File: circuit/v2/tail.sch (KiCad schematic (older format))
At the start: 44 parts, among them J11 UART, J19 LiPo, J25 USB_OTG, J9 DEBUG, Q1 Q_NMOS_GSD, SW1 SW_SPDT, U1 DWM1000, U2 EFM32HG222F64, U3 MC3630, U4 XC6215B332NR, U5 MCP73831-2-OT, Y1 32.768kHz CFPX-217 20ppm 7pF

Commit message: tail: minor tweaks
Signed-off-by: Gavan Fantom <gavan.fantom@unipart.io>
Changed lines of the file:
@@
 $EndComp
 $Comp
-L GND #PWR16
+L GND #PWR01
 U 1 1 58D90344
 P 8650 2850
-F 0 "#PWR16" H 8650 2600 50  0001 C CNN
+F 0 "#PWR01" H 8650 2600 50  0001 C CNN
 F 1 "GND" H 8650 2700 50  0000 C CNN
 F 2 "" H 8650 2850 50  0001 C CNN
@@
 $EndComp
 $Comp
-L +BATT #PWR12
+L +BATT #PWR02
 U 1 1 58D90443
 P 6950 2400
-F 0 "#PWR12" H 6950 2250 50  0001 C CNN
+F 0 "#PWR02" H 6950 2250 50  0001 C CNN
 F 1 "+BATT" H 6950 2540 50  0000 C CNN
 F 2 "" H 6950 2400 50  0001 C CNN
@@
 $EndComp
 $Comp
-L +BATT #PWR15
+L +BATT #PWR03
 U 1 1 58D91168
-P 8150 5100
-F 0 "#PWR15" H 8150 4950 50  0001 C CNN
-F 1 "+BATT" H 8150 5240 50  0000 C CNN
-F 2 "" H 8150 5100 50  0001 C CNN
-F 3 "" H 8150 5100 50  0001 C CNN
-	1    8150 5100
+P 7900 5100
+F 0 "#PWR03" H 7900 4950 50  0001 C CNN
+F 1 "+BATT" H 7900 5240 50  0000 C CNN
+F 2 "" H 7900 5100 50  0001 C CNN
+F 3 "" H 7900 5100 50  0001 C CNN
+	1    7900 5100
 	1    0    0    -1
 $EndComp
@@
 $EndComp
 $Comp
-L GND #PWR11
+L GND #PWR04
 U 1 1 58E2BE94
 P 6750 6700
-F 0 "#PWR11" H 6750 6450 50  0001 C CNN
+F 0 "#PWR04" H 6750 6450 50  0001 C CNN
 F 1 "GND" H 6750 6550 50  0000 C CNN
 F 2 "" H 6750 6700 50  0001 C CNN
@@
 $EndComp
 $Comp
-L GND #PWR7
+L GND #PWR05
 U 1 1 58E32705
 P 3750 2550
-F 0 "#PWR7" H 3750 2300 50  0001 C CNN
+F 0 "#PWR05" H 3750 2300 50  0001 C CNN
 F 1 "GND" H 3750 2400 50  0000 C CNN
 F 2 "" H 3750 2550 50  0001 C CNN
@@
 $EndComp
 $Comp
-L GND #PWR13
+L GND #PWR06
 U 1 1 58E5097D
 P 6950 3600
-F 0 "#PWR13" H 6950 3350 50  0001 C CNN
+F 0 "#PWR06" H 6950 3350 50  0001 C CNN
 F 1 "GND" H 6950 3450 50  0000 C CNN
 F 2 "" H 6950 3600 50  0001 C CNN
@@
 $EndComp
 $Comp
-L GND #PWR17
+L GND #PWR07
 U 1 1 58E581CA
 P 8750 4650
-F 0 "#PWR17" H 8750 4400 50  0001 C CNN
+F 0 "#PWR07" H 8750 4400 50  0001 C CNN
 F 1 "GND" H 8750 4500 50  0000 C CNN
 F 2 "" H 8750 4650 50  0001 C CNN
@@
 $EndComp
 $Comp
-L GND #PWR18
+L GND #PWR08
 U 1 1 58E5823C
 P 10300 5400
-F 0 "#PWR18" H 10300 5150 50  0001 C CNN
+F 0 "#PWR08" H 10300 5150 50  0001 C CNN
 F 1 "GND" H 10300 5250 50  0000 C CNN
 F 2 "" H 10300 5400 50  0001 C CNN
@@
 $EndComp
 $Comp
-L GND #PWR14
+L GND #PWR09
 U 1 1 58E62DAE
 P 7200 4150
-F 0 "#PWR14" H 7200 3900 50  0001 C CNN
+F 0 "#PWR09" H 7200 3900 50  0001 C CNN
 F 1 "GND" H 7200 4000 50  0000 C CNN
 F 2 "" H 7200 4150 50  0001 C CNN
@@
 $EndComp
 $Comp
-L GND #PWR10
+L GND #PWR010
 U 1 1 58ECBC0F
 P 5250 5000
-F 0 "#PWR10" H 5250 4750 50  0001 C CNN
+F 0 "#PWR010" H 5250 4750 50  0001 C CNN
 F 1 "GND" H 5250 4850 50  0000 C CNN
 F 2 "" H 5250 5000 50  0001 C CNN
@@
 $EndComp
 $Comp
-L GND #PWR6
+L GND #PWR011
 U 1 1 58ECC8B8
 P 2450 6250
-F 0 "#PWR6" H 2450 6000 50  0001 C CNN
+F 0 "#PWR011" H 2450 6000 50  0001 C CNN
 F 1 "GND" H 2450 6100 50  0000 C CNN
 F 2 "" H 2450 6250 50  0001 C CNN
@@
 $EndComp
 $Comp
-L GND #PWR2
+L GND #PWR012
 U 1 1 58ECC92E
 P 950 5150
-F 0 "#PWR2" H 950 4900 50  0001 C CNN
+F 0 "#PWR012" H 950 4900 50  0001 C CNN
 F 1 "GND" H 950 5000 50  0000 C CNN
 F 2 "" H 950 5150 50  0001 C CNN
@@
 $EndComp
 $Comp
-L GND #PWR5
+L GND #PWR013
 U 1 1 58ECCA91
 P 1700 3950
-F 0 "#PWR5" H 1700 3700 50  0001 C CNN
+F 0 "#PWR013" H 1700 3700 50  0001 C CNN
 F 1 "GND" H 1700 3800 50  0000 C CNN
 F 2 "" H 1700 3950 50  0001 C CNN
@@
 $EndComp
 $Comp
-L GND #PWR3
+L GND #PWR014
 U 1 1 58ECF8A7
 P 1050 7550
-F 0 "#PWR3" H 1050 7300 50  0001 C CNN
+F 0 "#PWR014" H 1050 7300 50  0001 C CNN
 F 1 "GND" H 1050 7400 50  0000 C CNN
 F 2 "" H 1050 7550 50  0001 C CNN
@@
 $EndComp
 $Comp
-L GND #PWR8
+L GND #PWR015
 U 1 1 58ED2393
 P 4250 5600
-F 0 "#PWR8" H 4250 5350 50  0001 C CNN
+F 0 "#PWR015" H 4250 5350 50  0001 C CNN
 F 1 "GND" H 4250 5450 50  0000 C CNN
 F 2 "" H 4250 5600 50  0001 C CNN
@@
 $EndComp
 $Comp
-L GND #PWR1
+L GND #PWR016
 U 1 1 58ED2E64
 P 900 6150
-F 0 "#PWR1" H 900 5900 50  0001 C CNN
+F 0 "#PWR016" H 900 5900 50  0001 C CNN
 F 1 "GND" H 900 6000 50  0000 C CNN
 F 2 "" H 900 6150 50  0001 C CNN
@@
 $EndComp
 $Comp
-L GND #PWR4
+L GND #PWR017
 U 1 1 58ED2EF0
 P 1400 6150
-F 0 "#PWR4" H 1400 5900 50  0001 C CNN
+F 0 "#PWR017" H 1400 5900 50  0001 C CNN
 F 1 "GND" H 1400 6000 50  0000 C CNN
 F 2 "" H 1400 6150 50  0001 C CNN
@@
 $EndComp
 $Comp
-L PWR_FLAG #FLG2
+L PWR_FLAG #FLG018
 U 1 1 58EFDE28
 P 10700 3950
-F 0 "#FLG2" H 10700 4025 50  0001 C CNN
+F 0 "#FLG018" H 10700 4025 50  0001 C CNN
 F 1 "PWR_FLAG" H 10700 4100 50  0000 C CNN
 F 2 "" H 10700 3950 50  0001 C CNN
@@
 $EndComp
 $Comp
-L PWR_FLAG #FLG1
+L PWR_FLAG #FLG019
 U 1 1 58F0C76B
 P 9950 5400
-F 0 "#FLG1" H 9950 5475 50  0001 C CNN
+F 0 "#FLG019" H 9950 5475 50  0001 C CNN
 F 1 "PWR_FLAG" H 9950 5550 50  0000 C CNN
 F 2 "" H 9950 5400 50  0001 C CNN
@@
 $EndComp
 $Comp
-L GND #PWR9
+L GND #PWR020
 U 1 1 590A2FEB
 P 4850 6800
-F 0 "#PWR9" H 4850 6550 50  0001 C CNN
+F 0 "#PWR020" H 4850 6550 50  0001 C CNN
 F 1 "GND" H 4850 6650 50  0000 C CNN
 F 2 "" H 4850 6800 50  0001 C CNN
@@
 	1500 5100 950  5100
 Wire Wire Line
-	5250 4600 5250 4700
-Wire Wire Line
-	5250 4700 5250 4800
-Wire Wire Line
-	5250 4800 5250 4900
-Wire Wire Line
-	5250 4900 5250 5000
+	5250 4600 5250 5000
 Wire Wire Line
 	9850 4250 9850 5050
@@
 	8750 3950 8750 4050
 Wire Wire Line
-	9150 4250 9300 4250
-Wire Wire Line
-	9300 4250 9850 4250
+	9150 4250 9850 4250
 Wire Wire Line
 	8250 4450 8250 4650
@@
 	8250 3950 8250 4250
 Wire Wire Line
-	8250 3950 8750 3950
-Wire Wire Line
-	8750 3950 9550 3950
-Wire Wire Line
-	9550 3950 10700 3950
+	8250 3950 10700 3950
 Wire Wire Line
 	9150 4450 9550 4450
@@
 	9300 4250 9300 4400
 Wire Wire Line
-	8250 4650 8350 4650
-Wire Wire Line
-	8350 4650 8750 4650
-Wire Wire Line
-	8750 4650 9300 4650
+	8250 4650 9300 4650
 Wire Wire Line
 	6950 3250 6650 3250
 Wire Wire Line
-	6950 3200 6950 3250
-Wire Wire Line
-	6950 3250 6950 3300
-Wire Wire Line
-	1000 1550 1150 1550
-Wire Wire Line
-	1150 1550 1500 1550
+	6950 3200 6950 3300
+Wire Wire Line
+	1000 1550 1500 1550
 Wire Wire Line
 	1500 1550 1500 1450
@@
 	3750 1250 3300 1250
 Wire Wire Line
-	3750 2550 3750 1250
-Wire Wire Line
-	3750 1250 3750 1050
-Wire Wire Line
-	3750 1050 3750 950
+	3750 2550 3750 950
 Wire Wire Line
 	3750 950  3300 950
@@
 	1300 1650 1500 1650
 Wire Wire Line
-	1300 1650 1300 1750
-Wire Wire Line
-	1300 1750 1300 2550
-Wire Wire Line
-	1300 2550 1800 2550
-Wire Wire Line
-	1800 2550 2800 2550
-Wire Wire Line
-	2800 2550 3550 2550
-Wire Wire Line
-	3550 2550 3750 2550
+	1300 1650 1300 2550
+Wire Wire Line
+	1300 2550 3750 2550
 Wire Wire Line
 	2800 2350 2800 2550
@@
 	6150 6800 6300 6800
 Wire Wire Line
-	6150 6600 6300 6600
-Wire Wire Line
-	6300 6600 6750 6600
+	6150 6600 6750 6600
 Wire Wire Line
 	4750 6700 4850 6700
@@
 	6150 7400 4750 7400
 Wire Wire Line
-	6150 6800 6150 7250
-Wire Wire Line
-	6150 7250 6150 7400
+	6150 6800 6150 7400
 Wire Wire Line
 	8150 2400 8150 2550
@@
 	8150 2550 8200 2550
 Wire Wire Line
-	6950 2400 7750 2400
-Wire Wire Line
-	7750 2400 8150 2400
-Wire Wire Line
-	8150 2400 8200 2400
+	6950 2400 8200 2400
 Wire Wire Line
 	10700 3950 10700 4800
@@
 	8800 5400 8800 5300
 Wire Wire Line
-	8800 5400 9950 5400
-Wire Wire Line
-	9950 5400 10300 5400
-Wire Wire Line
-	10300 5400 10400 5400
+	8800 5400 10400 5400
 Wire Wire Line
 	7750 2850 7750 2700
@@
 	9100 2850 9100 2700
 Wire Wire Line
-	7750 2850 8650 2850
-Wire Wire Line
-	8650 2850 9100 2850
-Wire Wire Line
-	9100 1550 9100 1700
-Wire Wire Line
-	9100 1700 9100 1850
-Wire Wire Line
-	9100 1850 9100 2000
-Wire Wire Line
-	9100 2000 9100 2400
-Wire Wire Line
-	9100 2400 9100 2500
+	7750 2850 9100 2850
+Wire Wire Line
+	9100 1550 9100 2500
 Wire Wire Line
 	7750 2500 7750 2400
 Wire Wire Line
-	1050 7550 1450 7550
-Wire Wire Line
-	1450 7550 1700 7550
-Wire Wire Line
-	1700 7550 1950 7550
-Wire Wire Line
-	1950 7550 2200 7550
-Wire Wire Line
-	2200 7550 2450 7550
-Wire Wire Line
-	2450 7550 2700 7550
-Wire Wire Line
-	2700 7550 2950 7550
-Wire Wire Line
-	1200 7250 1450 7250
-Wire Wire Line
-	1450 7250 1700 7250
-Wire Wire Line
-	1700 7250 1950 7250
-Wire Wire Line
-	1950 7250 2200 7250
-Wire Wire Line
-	2200 7250 2450 7250
-Wire Wire Line
-	2450 7250 2700 7250
-Wire Wire Line
-	2700 7250 2950 7250
+	1050 7550 2950 7550
+Wire Wire Line
+	1200 7250 2950 7250
 Wire Wire Line
 	1450 7250 1450 7300
@@
 	2950 6350 2950 6250
 Wire Wire Line
-	2850 6350 2900 6350
-Wire Wire Line
-	2900 6350 2950 6350
+	2850 6350 2950 6350
 Wire Wire Line
 	2850 6350 2850 6250
@@
 	2900 6350 2900 6450
 Wire Wire Line
-	1250 5800 1400 5800
-Wire Wire Line
-	1400 5800 1500 5800
+	1250 5800 1500 5800
 Wire Wire Line
 	1400 5800 1400 5950
@@
 	1050 5800 900  5800
 Wire Wire Line
-	900  5700 900  5800
-Wire Wire Line
-	900  5800 900  5950
+	900  5700 900  5950
 Wire Wire Line
 	1500 5700 900  5700
 Wire Wire Line
-	1800 2550 1800 3050
-Wire Wire Line
-	1800 3050 1800 3400
+	1800 2550 1800 3400
 Wire Wire Line
 	2700 3050 3050 3050
@@
 	2400 3050 2300 3050
 Wire Wire Line
-	3550 2550 3550 3050
-Wire Wire Line
-	3550 3050 3550 3400
+	3550 2550 3550 3400
 Wire Wire Line
 	1150 1750 1300 1750
@@
 	8800 5200 8700 5200
 Wire Wire Line
-	8150 5100 8300 5100
+	7900 5100 8300 5100
 NoConn ~ 8300 5300
+$Comp
+L PWR_FLAG #FLG021
+U 1 1 5BB39745
+P 8250 5100
+F 0 "#FLG021" H 8250 5175 50  0001 C CNN
+F 1 "PWR_FLAG" H 8250 5250 50  0000 C CNN
+F 2 "" H 8250 5100 50  0001 C CNN
+F 3 "" H 8250 5100 50  0001 C CNN
+	1    8250 5100
+	1    0    0    -1
+$EndComp
+Connection ~ 8250 5100
 $EndSCHEMATC

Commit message: tail: More detail for SSSS811101 slide switch
This involves correcting the schematic and the symbol to match up the
pin numbering with the datasheet, and to add a case/body connection.

Signed-off-by: Gavan Fantom <gavan.fantom@unipart.io>
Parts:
- SW1: footprint (none) -> tail:SWITCH_SSSS811101; symbol SW_SPDT -> SW_SPDT_SSSS8
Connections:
- net +BATT: now also SW1.1 (B); no longer SW1.3 (C)
- net GND: now also SW1.4 (Body)
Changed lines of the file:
@@
 L +BATT #PWR03
 U 1 1 58D91168
-P 7900 5100
-F 0 "#PWR03" H 7900 4950 50  0001 C CNN
-F 1 "+BATT" H 7900 5240 50  0000 C CNN
-F 2 "" H 7900 5100 50  0001 C CNN
-F 3 "" H 7900 5100 50  0001 C CNN
-	1    7900 5100
+P 8100 5300
+F 0 "#PWR03" H 8100 5150 50  0001 C CNN
+F 1 "+BATT" H 8100 5440 50  0000 C CNN
+F 2 "" H 8100 5300 50  0001 C CNN
+F 3 "" H 8100 5300 50  0001 C CNN
+	1    8100 5300
 	1    0    0    -1
 $EndComp
@@
 NoConn ~ 2350 6250
 $Comp
-L SW_SPDT SW1
+L SW_SPDT_SSSS8 SW1
 U 1 1 5BB37913
 P 8500 5200
-F 0 "SW1" H 8450 5050 50  0000 C CNN
-F 1 "SW_SPDT" H 8450 5400 50  0000 C CNN
-F 2 "" H 8500 5200 50  0001 C CNN
+F 0 "SW1" H 8450 5400 50  0000 C CNN
+F 1 "SW_SPDT" H 8500 5000 50  0000 C CNN
+F 2 "tail:SWITCH_SSSS811101" H 8500 5200 50  0001 C CNN
 F 3 "" H 8500 5200 50  0001 C CNN
 F 4 "ALPS" H 8500 5200 60  0001 C CNN "MFR"
@@
 F 7 "688-SSSS811101" H 8500 5200 60  0001 C CNN "SPN"
 	1    8500 5200
-	-1   0    0    1
+	-1   0    0    -1
 $EndComp
 Wire Wire Line
 	8800 5200 8700 5200
 Wire Wire Line
-	7900 5100 8300 5100
-NoConn ~ 8300 5300
+	8100 5300 8300 5300
+NoConn ~ 8300 5100
 $Comp
 L PWR_FLAG #FLG021
 U 1 1 5BB39745
-P 8250 5100
-F 0 "#FLG021" H 8250 5175 50  0001 C CNN
-F 1 "PWR_FLAG" H 8250 5250 50  0000 C CNN
-F 2 "" H 8250 5100 50  0001 C CNN
-F 3 "" H 8250 5100 50  0001 C CNN
-	1    8250 5100
-	1    0    0    -1
-$EndComp
-Connection ~ 8250 5100
+P 8100 5300
+F 0 "#FLG021" H 8100 5375 50  0001 C CNN
+F 1 "PWR_FLAG" H 8100 5450 50  0000 C CNN
+F 2 "" H 8100 5300 50  0001 C CNN
+F 3 "" H 8100 5300 50  0001 C CNN
+	1    8100 5300
+	-1   0    0    1
+$EndComp
+Connection ~ 8100 5300
+$Comp
+L GND #PWR022
+U 1 1 5BB3B459
+P 8750 5450
+F 0 "#PWR022" H 8750 5200 50  0001 C CNN
+F 1 "GND" H 8750 5300 50  0000 C CNN
+F 2 "" H 8750 5450 50  0001 C CNN
+F 3 "" H 8750 5450 50  0001 C CNN
+	1    8750 5450
+	1    0    0    -1
+$EndComp
+Wire Wire Line
+	8700 5300 8750 5300
+Wire Wire Line
+	8750 5300 8750 5450
 $EndSCHEMATC

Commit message: tail: Route PCB
Signed-off-by: Gavan Fantom <gavan.fantom@unipart.io>
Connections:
- net +BATT: now also SW1.2 (C); no longer SW1.1 (B)
- net at C18.1, J19.1 (P1), U5.3 (Vbat): now also SW1.1 (B); no longer SW1.2 (C)
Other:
- moved on the sheet: SW1
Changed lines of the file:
@@
 L +BATT #PWR03
 U 1 1 58D91168
-P 8100 5300
-F 0 "#PWR03" H 8100 5150 50  0001 C CNN
-F 1 "+BATT" H 8100 5440 50  0000 C CNN
-F 2 "" H 8100 5300 50  0001 C CNN
-F 3 "" H 8100 5300 50  0001 C CNN
-	1    8100 5300
+P 8000 5100
+F 0 "#PWR03" H 8000 4950 50  0001 C CNN
+F 1 "+BATT" H 8000 5240 50  0000 C CNN
+F 2 "" H 8000 5100 50  0001 C CNN
+F 3 "" H 8000 5100 50  0001 C CNN
+	1    8000 5100
 	1    0    0    -1
 $EndComp
@@
 L SW_SPDT_SSSS8 SW1
 U 1 1 5BB37913
-P 8500 5200
-F 0 "SW1" H 8450 5400 50  0000 C CNN
-F 1 "SW_SPDT" H 8500 5000 50  0000 C CNN
-F 2 "tail:SWITCH_SSSS811101" H 8500 5200 50  0001 C CNN
-F 3 "" H 8500 5200 50  0001 C CNN
-F 4 "ALPS" H 8500 5200 60  0001 C CNN "MFR"
-F 5 "SSSS811101" H 8500 5200 60  0001 C CNN "MPN"
-F 6 "Mouser" H 8500 5200 60  0001 C CNN "SPR"
-F 7 "688-SSSS811101" H 8500 5200 60  0001 C CNN "SPN"
-	1    8500 5200
-	-1   0    0    -1
+P 8500 5100
+F 0 "SW1" H 8450 5300 50  0000 C CNN
+F 1 "SW_SPDT" H 8500 4900 50  0000 C CNN
+F 2 "tail:SWITCH_SSSS811101" H 8500 5100 50  0001 C CNN
+F 3 "" H 8500 5100 50  0001 C CNN
+F 4 "ALPS" H 8500 5100 60  0001 C CNN "MFR"
+F 5 "SSSS811101" H 8500 5100 60  0001 C CNN "MPN"
+F 6 "Mouser" H 8500 5100 60  0001 C CNN "SPR"
+F 7 "688-SSSS811101" H 8500 5100 60  0001 C CNN "SPN"
+	1    8500 5100
+	1    0    0    -1
 $EndComp
 Wire Wire Line
 	8800 5200 8700 5200
 Wire Wire Line
-	8100 5300 8300 5300
-NoConn ~ 8300 5100
+	8000 5100 8300 5100
+NoConn ~ 8700 5000
 $Comp
 L PWR_FLAG #FLG021
 U 1 1 5BB39745
-P 8100 5300
-F 0 "#FLG021" H 8100 5375 50  0001 C CNN
-F 1 "PWR_FLAG" H 8100 5450 50  0000 C CNN
-F 2 "" H 8100 5300 50  0001 C CNN
-F 3 "" H 8100 5300 50  0001 C CNN
-	1    8100 5300
+P 8000 5100
+F 0 "#FLG021" H 8000 5175 50  0001 C CNN
+F 1 "PWR_FLAG" H 8000 5250 50  0000 C CNN
+F 2 "" H 8000 5100 50  0001 C CNN
+F 3 "" H 8000 5100 50  0001 C CNN
+	1    8000 5100
 	-1   0    0    1
 $EndComp
-Connection ~ 8100 5300
+Connection ~ 8000 5100
 $Comp
 L GND #PWR022
 U 1 1 5BB3B459
-P 8750 5450
-F 0 "#PWR022" H 8750 5200 50  0001 C CNN
-F 1 "GND" H 8750 5300 50  0000 C CNN
-F 2 "" H 8750 5450 50  0001 C CNN
-F 3 "" H 8750 5450 50  0001 C CNN
-	1    8750 5450
-	1    0    0    -1
-$EndComp
-Wire Wire Line
-	8700 5300 8750 5300
-Wire Wire Line
-	8750 5300 8750 5450
+P 8250 5350
+F 0 "#PWR022" H 8250 5100 50  0001 C CNN
+F 1 "GND" H 8250 5200 50  0000 C CNN
+F 2 "" H 8250 5350 50  0001 C CNN
+F 3 "" H 8250 5350 50  0001 C CNN
+	1    8250 5350
+	1    0    0    -1
+$EndComp
+Wire Wire Line
+	8300 5200 8250 5200
+Wire Wire Line
+	8250 5200 8250 5350
 $EndSCHEMATC

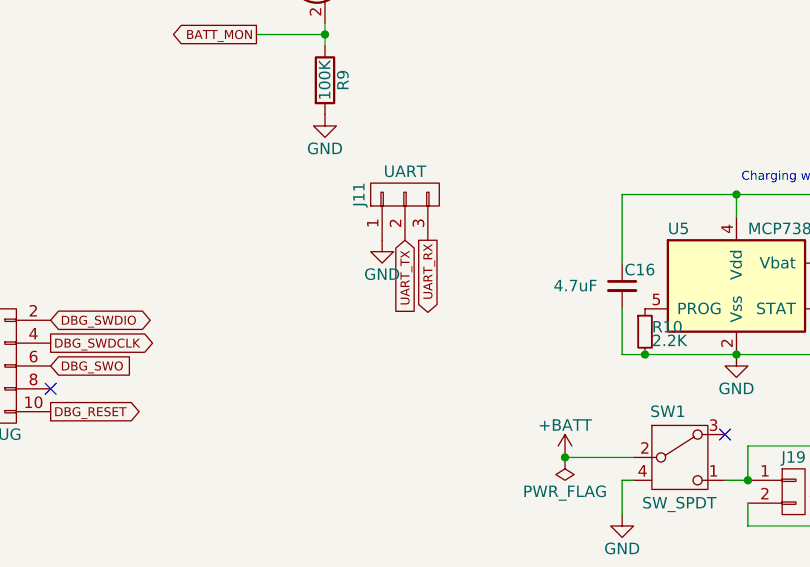
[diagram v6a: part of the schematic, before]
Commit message: tail: Change UART connector to right angle
... and move things around to make it fit.

Signed-off-by: Gavan Fantom <gavan.fantom@unipart.io>
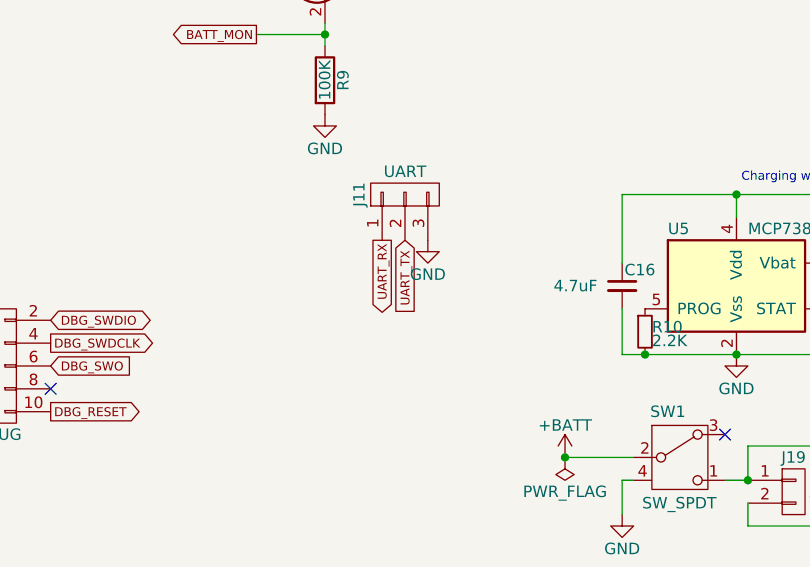
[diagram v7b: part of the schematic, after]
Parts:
- J11: footprint Pin_Headers:Pin_Header_Straight_1x03_Pitch2.54mm -> Pin_Headers:Pin_Header_Angled_1x03_Pitch2.54mm; MPN 2211S-03G -> MC34747; SPN 1593412 -> 1593427
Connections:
- net GND: now also J11.3 (P3); no longer J11.1 (P1)
- net UART_RX: now also J11.1 (P1); no longer J11.3 (P3)
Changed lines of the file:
@@
 F 0 "J11" H 7300 4150 50  0000 C CNN
 F 1 "UART" V 7400 3950 50  0000 C CNN
-F 2 "Pin_Headers:Pin_Header_Straight_1x03_Pitch2.54mm" H 7300 3950 50  0001 C CNN
+F 2 "Pin_Headers:Pin_Header_Angled_1x03_Pitch2.54mm" H 7300 3950 50  0001 C CNN
 F 3 "" H 7300 3950 50  0001 C CNN
 F 4 "Multicomp" H 0   0   50  0001 C CNN "MFR"
-F 5 "2211S-03G" H 0   0   50  0001 C CNN "MPN"
-F 6 "Farnell" H 0   0   50  0001 C CNN "SPR"
-F 7 "1593412" H 0   0   50  0001 C CNN "SPN"
+F 5 "MC34747" H 0   0   50  0001 C CNN "MPN"
+F 6 "Farnell" H 0   0   50  0001 C CNN "SPR"
+F 7 "1593427" H 0   0   50  0001 C CNN "SPN"
 F 8 "-" H 0   0   50  0001 C CNN "SPURL"
 	1    7300 3950
@@
 L GND #PWR09
 U 1 1 58E62DAE
-P 7200 4150
-F 0 "#PWR09" H 7200 3900 50  0001 C CNN
-F 1 "GND" H 7200 4000 50  0000 C CNN
-F 2 "" H 7200 4150 50  0001 C CNN
-F 3 "" H 7200 4150 50  0001 C CNN
-	1    7200 4150
+P 7400 4150
+F 0 "#PWR09" H 7400 3900 50  0001 C CNN
+F 1 "GND" H 7400 4000 50  0000 C CNN
+F 2 "" H 7400 4150 50  0001 C CNN
+F 3 "" H 7400 4150 50  0001 C CNN
+	1    7400 4150
 	1    0    0    -1
 $EndComp
@@
 Text GLabel 7300 4150 3    39   Input ~ 0
 UART_TX
-Text GLabel 7400 4150 3    39   Output ~ 0
+Text GLabel 7200 4150 3    39   Output ~ 0
 UART_RX
 Text GLabel 3050 6250 3    39   Output ~ 0
